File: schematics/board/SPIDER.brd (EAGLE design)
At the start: 68 x 100 mm, 8 parts

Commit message: Папка с платами
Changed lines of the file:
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@@
 <setting verticaltext="up"/>
 </settings>
-<grid distance="0.1" unitdist="mm" unit="mm" style="lines" multiple="1" display="yes" altdistance="0.001" altunitdist="mm" altunit="mm"/>
+<grid distance="1" unitdist="mm" unit="mm" style="lines" multiple="1" display="no" altdistance="0.01" altunitdist="mm" altunit="mm"/>
 <layers>
 <layer number="1" name="Top" color="4" fill="1" visible="yes" active="yes"/>
@@
 <board>
 <plain>
-<hole x="4" y="4" drill="6"/>
-<hole x="64" y="4" drill="6"/>
-<hole x="64" y="96" drill="6"/>
-<hole x="4" y="96" drill="6"/>
+<hole x="4" y="4" drill="3.5"/>
+<hole x="64" y="4" drill="3.5"/>
+<hole x="64" y="96" drill="3.5"/>
+<hole x="4" y="96" drill="3.5"/>
 <wire x1="0" y1="0" x2="8" y2="0" width="0.1" layer="20"/>
 <wire x1="8" y1="0" x2="8" y2="16.27193125" width="0.1" layer="20"/>

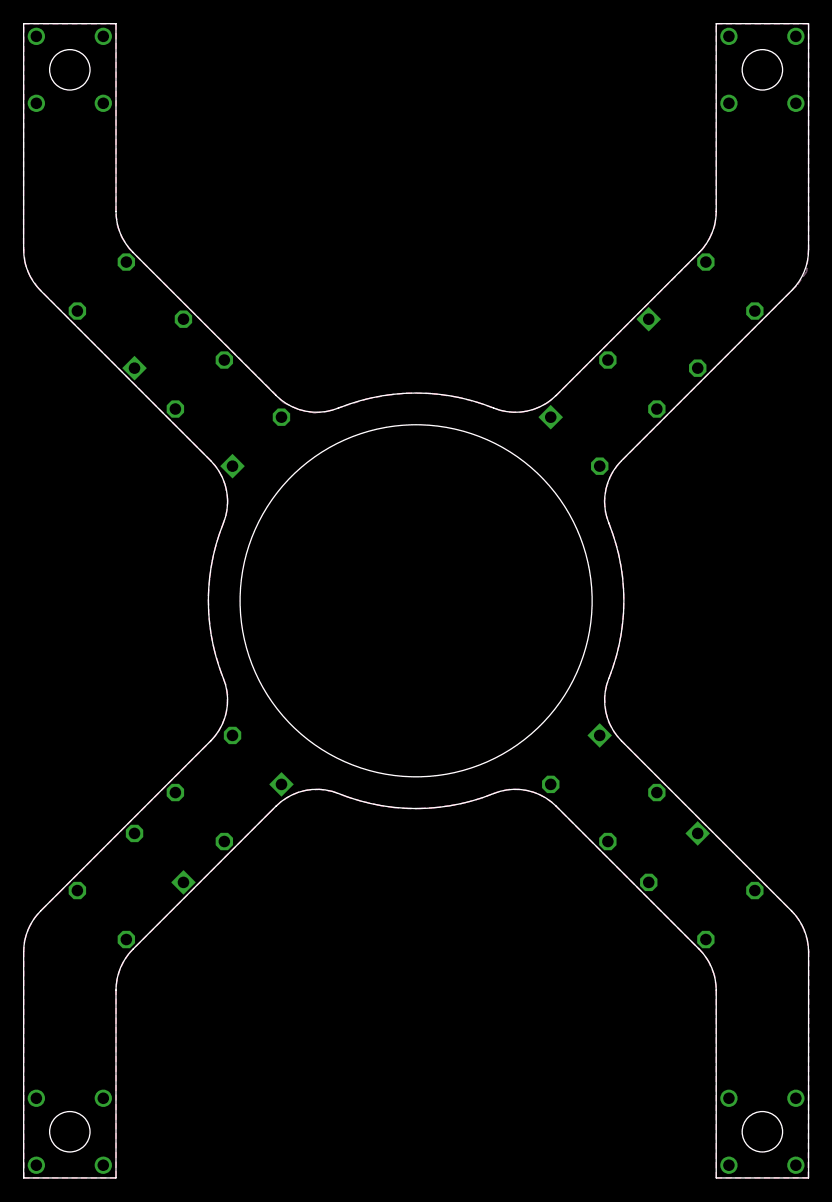
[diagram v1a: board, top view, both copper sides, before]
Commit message: Обновлен список плат, работа над платой ПН
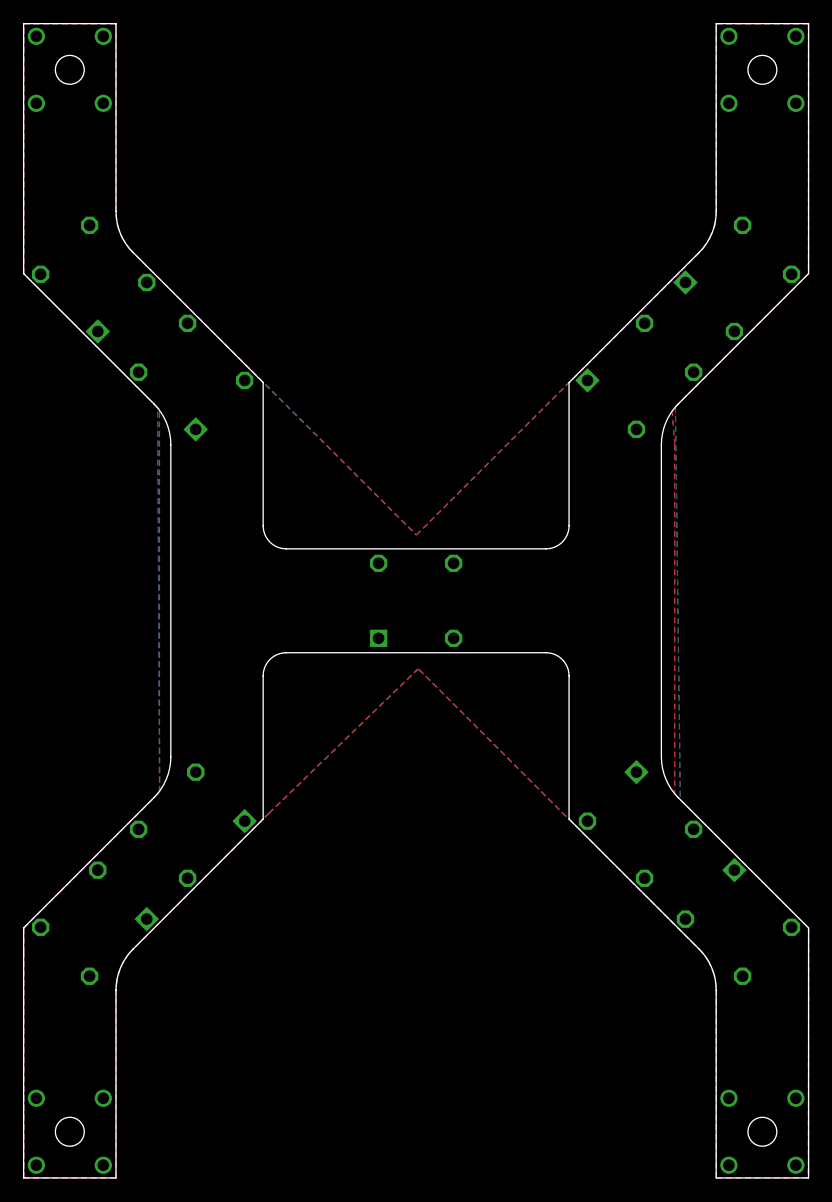
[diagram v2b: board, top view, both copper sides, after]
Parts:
- added U$5: KCONNECTQUAD-, CanCubeSat:KCONNECT-_QUAD
- moved U$21 4.50 mm to (53.4, 30.6)
- moved U$19 4.50 mm to (14.6, 30.6)
- moved U$4 4.50 mm to (53.4, 69.4)
- moved U$2 4.50 mm to (14.6, 69.4)
- moved U$18 4.50 mm to (6.07, 22.1)
- moved U$1 4.50 mm to (6.07, 77.9)
- moved U$20 4.50 mm to (61.9, 22.1)
- moved U$3 4.50 mm to (61.9, 77.9)
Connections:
- new net CMD: U$5.1, U$5.2, U$5.3, U$5.4
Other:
- outline, holes or cut-outs redrawn
